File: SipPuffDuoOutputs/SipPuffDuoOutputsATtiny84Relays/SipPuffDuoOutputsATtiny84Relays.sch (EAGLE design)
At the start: 19 parts, among them U1 ATTINY84-20PU, U2 AQY212EH, U3 AQY212EH

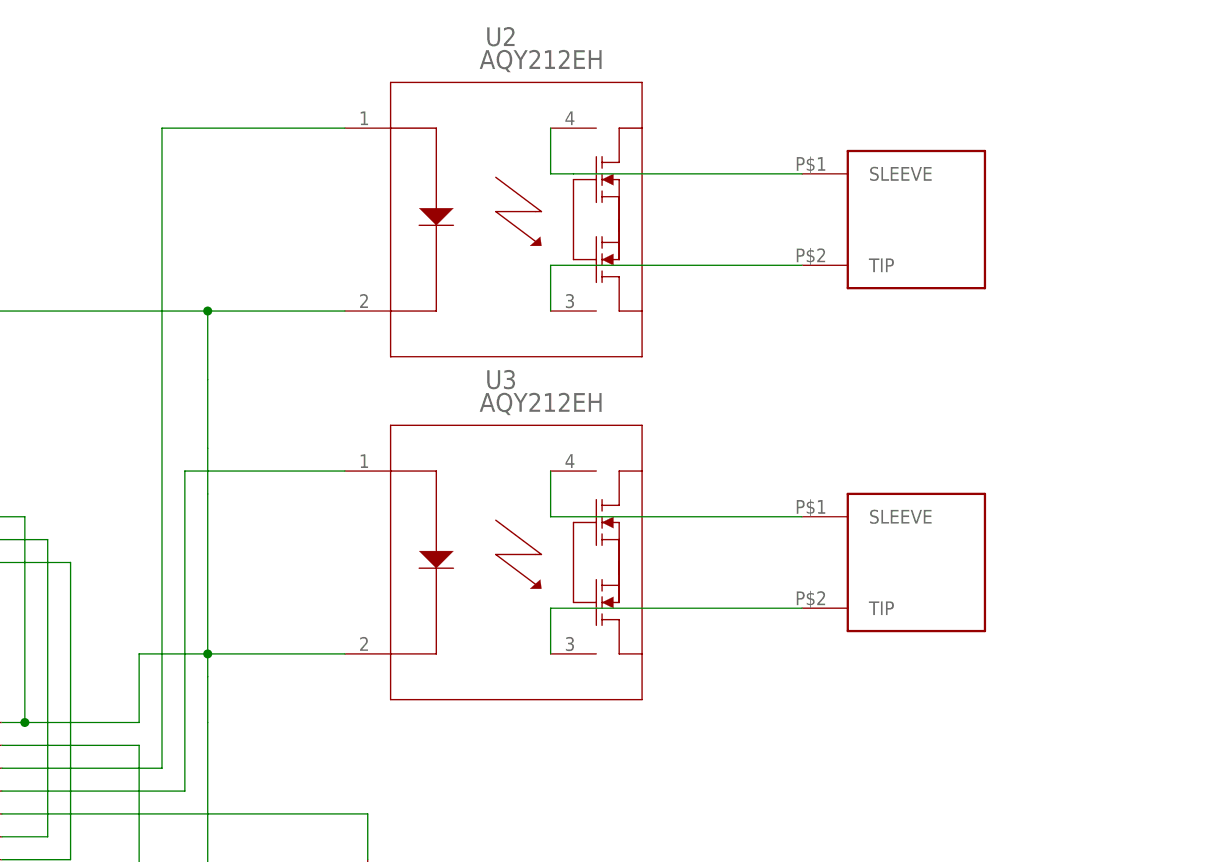
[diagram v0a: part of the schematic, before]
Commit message: Changed resistors size
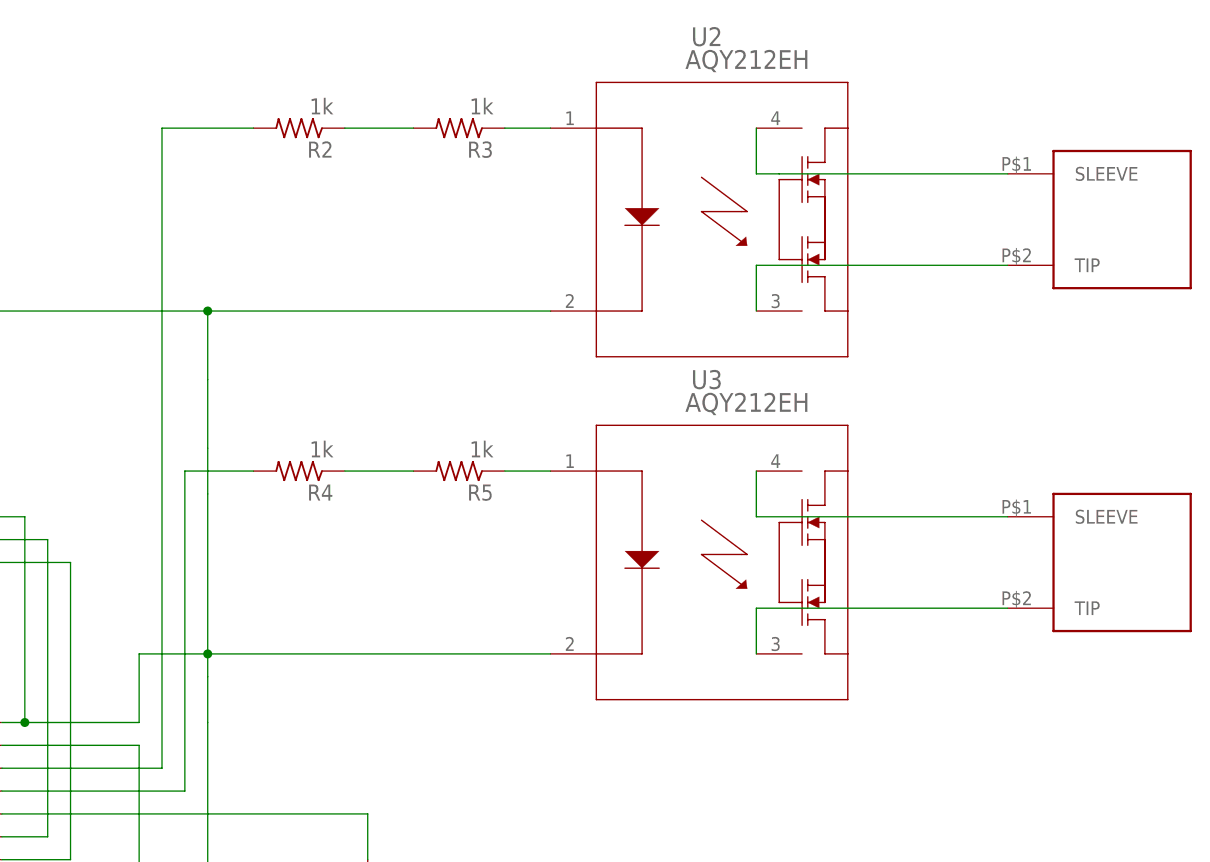
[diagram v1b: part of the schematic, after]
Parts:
- added R2, R3, R4, R5: 1k, MMC Eagle:RESISTOR_R-US_
- R1: device MMC Eagle:RESISTOR_R-US_0204/5 -> MMC Eagle:RESISTOR_R-US_
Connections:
- new net N$19: R2.1, R3.2
- new net N$20: R3.1, U2.1
- new net N$21: R4.1, R5.2
- new net N$22: R5.1, U3.1
- net N$2: now also R2.2; no longer U2.1
- net N$4: now also R4.2; no longer U3.1
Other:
- moved on the sheet: U2, U3
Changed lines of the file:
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@@
 <part name="U1" library="MMC Eagle" library_urn="urn:adsk.eagle:library:3491419" deviceset="ATTINY84-20PU" device="" package3d_urn="urn:adsk.eagle:package:4704288/2"/>
 <part name="D1" library="MMC Eagle" library_urn="urn:adsk.eagle:library:3491419" deviceset="LED" device="5MM" package3d_urn="urn:adsk.eagle:package:3634149/2"/>
-<part name="R1" library="MMC Eagle" library_urn="urn:adsk.eagle:library:3491419" deviceset="RESISTOR_R-US_" device="0204/5" package3d_urn="urn:adsk.eagle:package:3491543/2" value="1k"/>
+<part name="R1" library="MMC Eagle" library_urn="urn:adsk.eagle:library:3491419" deviceset="RESISTOR_R-US_" device="" package3d_urn="urn:adsk.eagle:package:5426338/2" value="1k"/>
 <part name="GND6" library="MMC Eagle" library_urn="urn:adsk.eagle:library:3491419" deviceset="GND" device=""/>
 <part name="U$1" library="MMC Eagle" library_urn="urn:adsk.eagle:library:3491419" deviceset="HEADER_2X03" device="" package3d_urn="urn:adsk.eagle:package:4704386/2"/>
@@
 <part name="U3" library="MMC Eagle" library_urn="urn:adsk.eagle:library:3491419" deviceset="AQY212EH" device="" package3d_urn="urn:adsk.eagle:package:4126881/2"/>
 <part name="U$5" library="MMC Eagle" library_urn="urn:adsk.eagle:library:3491419" deviceset="HEADER_1X02" device="" package3d_urn="urn:adsk.eagle:package:4737896/2"/>
+<part name="R2" library="MMC Eagle" library_urn="urn:adsk.eagle:library:3491419" deviceset="RESISTOR_R-US_" device="" package3d_urn="urn:adsk.eagle:package:5426338/2" value="1k"/>
+<part name="R3" library="MMC Eagle" library_urn="urn:adsk.eagle:library:3491419" deviceset="RESISTOR_R-US_" device="" package3d_urn="urn:adsk.eagle:package:5426338/2" value="1k"/>
+<part name="R4" library="MMC Eagle" library_urn="urn:adsk.eagle:library:3491419" deviceset="RESISTOR_R-US_" device="" package3d_urn="urn:adsk.eagle:package:5426338/2" value="1k"/>
+<part name="R5" library="MMC Eagle" library_urn="urn:adsk.eagle:library:3491419" deviceset="RESISTOR_R-US_" device="" package3d_urn="urn:adsk.eagle:package:5426338/2" value="1k"/>
 </parts>
 <sheets>
@@
 <instance part="ON_OF" gate="G$1" x="165.1" y="88.9"/>
 <instance part="BUZZER_SW" gate="G$1" x="294.64" y="17.78" rot="R270"/>
-<instance part="U$3" gate="G$1" x="381" y="96.52"/>
-<instance part="U$4" gate="G$1" x="381" y="58.42"/>
-<instance part="U2" gate="A" x="314.96" y="106.68"/>
-<instance part="U3" gate="A" x="314.96" y="68.58"/>
+<instance part="U$3" gate="G$1" x="403.86" y="96.52"/>
+<instance part="U$4" gate="G$1" x="403.86" y="58.42"/>
+<instance part="U2" gate="A" x="337.82" y="106.68"/>
+<instance part="U3" gate="A" x="337.82" y="68.58"/>
 <instance part="U$5" gate="G$1" x="109.22" y="12.7" rot="R180"/>
+<instance part="R2" gate="G$1" x="312.42" y="106.68" rot="R180"/>
+<instance part="R3" gate="G$1" x="330.2" y="106.68" rot="R180"/>
+<instance part="R4" gate="G$1" x="312.42" y="68.58" rot="R180"/>
+<instance part="R5" gate="G$1" x="330.2" y="68.58" rot="R180"/>
 </instances>
 <busses>
@@
 <junction x="302.26" y="-10.16"/>
 <pinref part="U2" gate="A" pin="2"/>
-<wire x1="317.5" y1="86.36" x2="302.26" y2="86.36" width="0.1524" layer="91"/>
+<wire x1="340.36" y1="86.36" x2="302.26" y2="86.36" width="0.1524" layer="91"/>
 <junction x="302.26" y="86.36"/>
 <pinref part="U3" gate="A" pin="2"/>
-<wire x1="317.5" y1="48.26" x2="302.26" y2="48.26" width="0.1524" layer="91"/>
+<wire x1="340.36" y1="48.26" x2="302.26" y2="48.26" width="0.1524" layer="91"/>
 <pinref part="SOLO_DUO" gate="A" pin="P"/>
 <wire x1="81.28" y1="63.5" x2="78.74" y2="63.5" width="0.1524" layer="91"/>
@@
 <wire x1="279.4" y1="35.56" x2="297.18" y2="35.56" width="0.1524" layer="91"/>
 <wire x1="297.18" y1="35.56" x2="297.18" y2="106.68" width="0.1524" layer="91"/>
-<pinref part="U2" gate="A" pin="1"/>
-<wire x1="297.18" y1="106.68" x2="317.5" y2="106.68" width="0.1524" layer="91"/>
+<pinref part="R2" gate="G$1" pin="2"/>
+<wire x1="307.34" y1="106.68" x2="297.18" y2="106.68" width="0.1524" layer="91"/>
 </segment>
 </net>
@@
 <wire x1="279.4" y1="33.02" x2="299.72" y2="33.02" width="0.1524" layer="91"/>
 <wire x1="299.72" y1="33.02" x2="299.72" y2="68.58" width="0.1524" layer="91"/>
-<pinref part="U3" gate="A" pin="1"/>
-<wire x1="299.72" y1="68.58" x2="317.5" y2="68.58" width="0.1524" layer="91"/>
+<pinref part="R4" gate="G$1" pin="2"/>
+<wire x1="307.34" y1="68.58" x2="299.72" y2="68.58" width="0.1524" layer="91"/>
 </segment>
 </net>
@@
 <segment>
 <pinref part="U2" gate="A" pin="4"/>
-<wire x1="340.36" y1="106.68" x2="340.36" y2="101.6" width="0.1524" layer="91"/>
-<wire x1="340.36" y1="101.6" x2="342.9" y2="101.6" width="0.1524" layer="91"/>
+<wire x1="363.22" y1="106.68" x2="363.22" y2="101.6" width="0.1524" layer="91"/>
+<wire x1="363.22" y1="101.6" x2="365.76" y2="101.6" width="0.1524" layer="91"/>
 <pinref part="U$3" gate="G$1" pin="SLEEVE"/>
-<wire x1="342.9" y1="101.6" x2="368.3" y2="101.6" width="0.1524" layer="91"/>
+<wire x1="365.76" y1="101.6" x2="391.16" y2="101.6" width="0.1524" layer="91"/>
 </segment>
 </net>
@@
 <segment>
 <pinref part="U2" gate="A" pin="3"/>
-<wire x1="340.36" y1="86.36" x2="340.36" y2="91.44" width="0.1524" layer="91"/>
+<wire x1="363.22" y1="86.36" x2="363.22" y2="91.44" width="0.1524" layer="91"/>
 <pinref part="U$3" gate="G$1" pin="TIP"/>
-<wire x1="340.36" y1="91.44" x2="368.3" y2="91.44" width="0.1524" layer="91"/>
+<wire x1="363.22" y1="91.44" x2="391.16" y2="91.44" width="0.1524" layer="91"/>
 </segment>
 </net>
@@
 <pinref part="U3" gate="A" pin="4"/>
 <pinref part="U$4" gate="G$1" pin="SLEEVE"/>
-<wire x1="340.36" y1="68.58" x2="340.36" y2="63.5" width="0.1524" layer="91"/>
-<wire x1="340.36" y1="63.5" x2="368.3" y2="63.5" width="0.1524" layer="91"/>
+<wire x1="363.22" y1="68.58" x2="363.22" y2="63.5" width="0.1524" layer="91"/>
+<wire x1="363.22" y1="63.5" x2="391.16" y2="63.5" width="0.1524" layer="91"/>
 </segment>
 </net>
@@
 <segment>
 <pinref part="U3" gate="A" pin="3"/>
-<wire x1="340.36" y1="48.26" x2="340.36" y2="53.34" width="0.1524" layer="91"/>
+<wire x1="363.22" y1="48.26" x2="363.22" y2="53.34" width="0.1524" layer="91"/>
 <pinref part="U$4" gate="G$1" pin="TIP"/>
-<wire x1="340.36" y1="53.34" x2="368.3" y2="53.34" width="0.1524" layer="91"/>
+<wire x1="363.22" y1="53.34" x2="391.16" y2="53.34" width="0.1524" layer="91"/>
 </segment>
 </net>
@@
 </segment>
 </net>
+<net name="N$19" class="0">
+<segment>
+<pinref part="R3" gate="G$1" pin="2"/>
+<pinref part="R2" gate="G$1" pin="1"/>
+<wire x1="325.12" y1="106.68" x2="317.5" y2="106.68" width="0.1524" layer="91"/>
+</segment>
+</net>
+<net name="N$20" class="0">
+<segment>
+<pinref part="U2" gate="A" pin="1"/>
+<pinref part="R3" gate="G$1" pin="1"/>
+<wire x1="340.36" y1="106.68" x2="335.28" y2="106.68" width="0.1524" layer="91"/>
+</segment>
+</net>
+<net name="N$21" class="0">
+<segment>
+<pinref part="R4" gate="G$1" pin="1"/>
+<pinref part="R5" gate="G$1" pin="2"/>
+<wire x1="317.5" y1="68.58" x2="325.12" y2="68.58" width="0.1524" layer="91"/>
+</segment>
+</net>
+<net name="N$22" class="0">
+<segment>
+<pinref part="R5" gate="G$1" pin="1"/>
+<pinref part="U3" gate="A" pin="1"/>
+<wire x1="335.28" y1="68.58" x2="340.36" y2="68.58" width="0.1524" layer="91"/>
+</segment>
+</net>
